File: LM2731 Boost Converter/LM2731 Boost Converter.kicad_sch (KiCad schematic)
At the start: 17 parts, among them J1 USB_C_Receptacle_PowerOnly_6P, SW1 SW_SPDT, U1 LM2731YMF

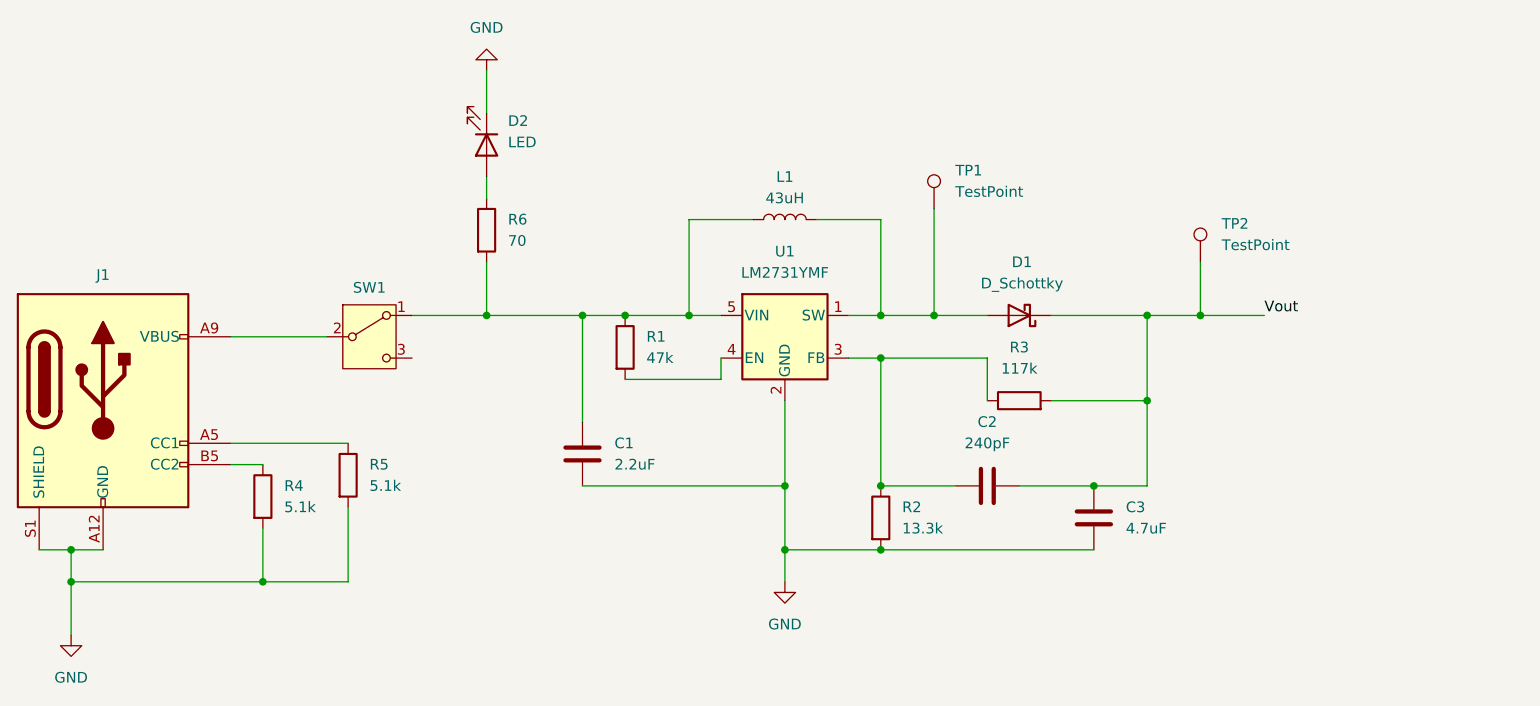
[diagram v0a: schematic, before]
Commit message: Finished sourcing parts and assigning footprints. Had to add the footprint for the inductor.
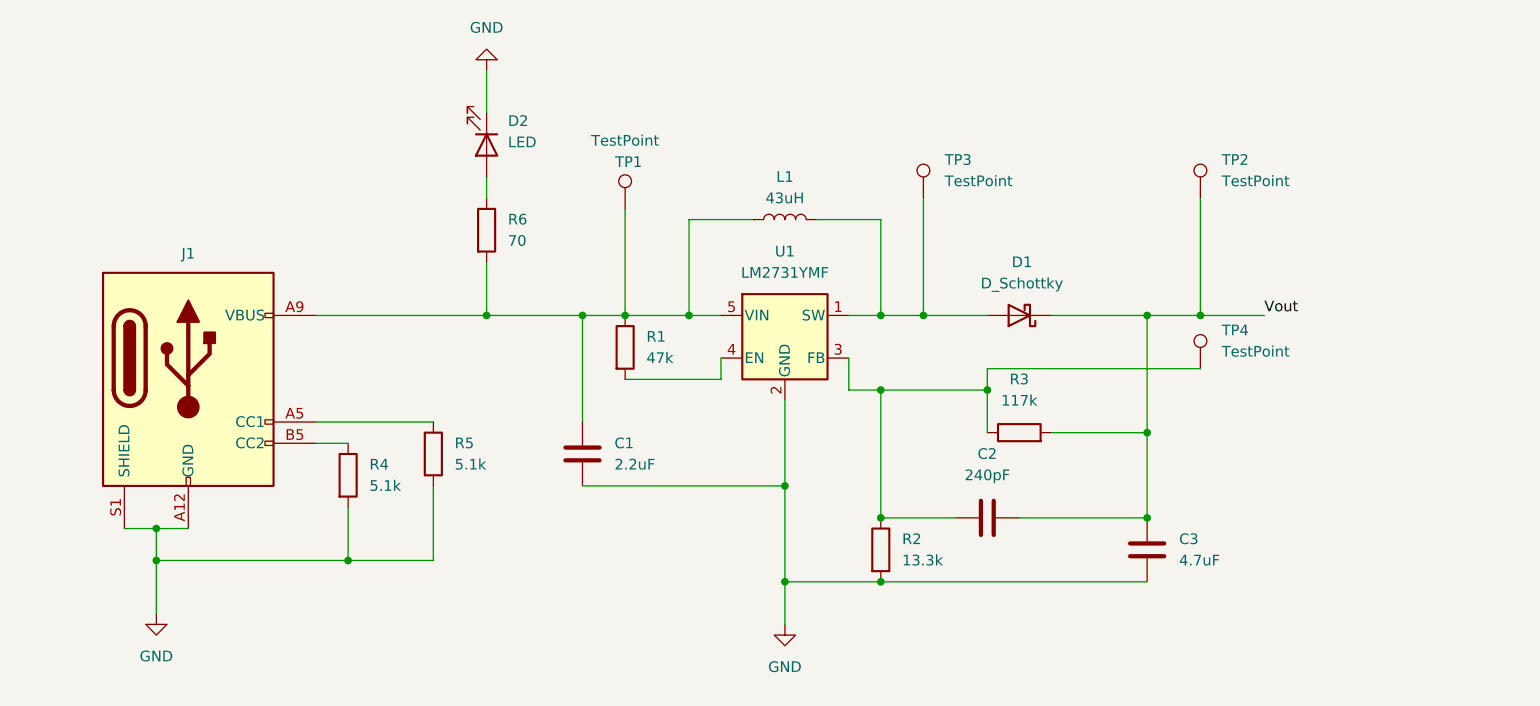
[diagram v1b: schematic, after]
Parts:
- removed SW1: SW_SPDT, symbol Switch:SW_SPDT
- added TP3, TP4: TestPoint, TestPoint:TestPoint_Keystone_5000-5004_Miniature, symbol Connector:TestPoint
- C1: Part Number  LMK316AB7226KL-TR -> LMF316B7225KLHT
- C2: footprint (none) -> Capacitor_SMD:C_0201_0603Metric_Pad0.64x0.40mm_HandSolder; Part Number  (none) -> KGM15AR71C221KT
- C3: footprint (none) -> Capacitor_SMD:C_1210_3225Metric_Pad1.33x2.70mm_HandSolder; Part Number  (none) -> LMK325BJ475KD-T
- L1: footprint (none) -> Inductor_SMD:IND_ASPI-8040S-430M-T; Part Number  (none) -> ASPI-8040S-430M-T
- R1: footprint (none) -> Resistor_SMD:R_0603_1608Metric_Pad0.98x0.95mm_HandSolder; Part Number  (none) -> RC0603FR-0747KL
- R2: footprint (none) -> Resistor_SMD:R_0603_1608Metric_Pad0.98x0.95mm_HandSolder; Part Number  (none) -> RC0603FR-0713K3L
- R3: footprint (none) -> Resistor_SMD:R_0603_1608Metric_Pad0.98x0.95mm_HandSolder; Part Number  (none) -> RT0603DRE07117KL
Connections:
- net at C1.1, L1.1, R1.1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: now also J1.A9 (VBUS), J1.B9 (VBUS), TP1.1
- net at D1.2 (A), L1.2, U1.1 (SW): now also TP3.1; no longer TP1.1
- net at C2.2, R2.1, R3.1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: now also TP4.1
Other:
- moved on the sheet: C2, C3, J1, R2, R3, R4, R5, TP1, TP2

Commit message: Started the PCB layout. Updated the Keystone 5000 test point to reflect the
correct part.
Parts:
- C2: footprint Capacitor_SMD:C_0201_0603Metric_Pad0.64x0.40mm_HandSolder -> Capacitor_SMD:C_0603_1608Metric_Pad1.08x0.95mm_HandSolder
- TP1, TP2, TP3, TP4: footprint TestPoint:TestPoint_Keystone_5000-5004_Miniature -> TestPoint:KEYSTONE_5000
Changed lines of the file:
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@@
 			)
 		)
-		(property "Footprint" "TestPoint:TestPoint_Keystone_5000-5004_Miniature"
+		(property "Footprint" "TestPoint:KEYSTONE_5000"
 			(at 180.34 71.12 0)
 			(effects
@@
 			)
 		)
-		(property "Footprint" "TestPoint:TestPoint_Keystone_5000-5004_Miniature"
+		(property "Footprint" "TestPoint:KEYSTONE_5000"
 			(at 213.36 91.44 0)
 			(effects
@@
 			)
 		)
-		(property "Footprint" "TestPoint:TestPoint_Keystone_5000-5004_Miniature"
+		(property "Footprint" "TestPoint:KEYSTONE_5000"
 			(at 144.78 72.39 0)
 			(effects
@@
 			)
 		)
-		(property "Footprint" "Capacitor_SMD:C_0201_0603Metric_Pad0.64x0.40mm_HandSolder"
+		(property "Footprint" "Capacitor_SMD:C_0603_1608Metric_Pad1.08x0.95mm_HandSolder"
 			(at 179.07 110.1852 0)
 			(effects
@@
 			)
 		)
-		(property "Footprint" "TestPoint:TestPoint_Keystone_5000-5004_Miniature"
+		(property "Footprint" "TestPoint:KEYSTONE_5000"
 			(at 213.36 71.12 0)
 			(effects

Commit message: Laid out parts and added a output screw terminal.
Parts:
- added J2: Screw_Terminal_01x02, TerminalBlock_Phoenix:PHOENIX_1725656, symbol Connector:Screw_Terminal_01x02
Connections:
- net GND: now also J2.2 (Pin_2)
- net Vout: now also J2.1 (Pin_1)
- net Vin: now reaches C1.1, J1.A9 (VBUS), J1.B9 (VBUS), L1.1, R1.1, R6.2, TP1.1, U1.5 (VIN)
- net SwitchNode: now reaches D1.2 (A), L1.2, TP3.1, U1.1 (SW)
- net Feedback: now reaches C2.2, R2.1, R3.1, TP4.1, U1.3 (FB)
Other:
- moved on the sheet: C2, C3, D1, R3, TP2, TP3, TP4

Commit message: Finished board layout.
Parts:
- U1: footprint Package_TO_SOT_SMD:SOT-23-5_HandSoldering -> Package_TO_SOT_SMD:SOT-23-5
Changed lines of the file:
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@@
 			)
 		)
-		(property "Footprint" "Package_TO_SOT_SMD:SOT-23-5_HandSoldering"
+		(property "Footprint" "Package_TO_SOT_SMD:SOT-23-5"
 			(at 160.02 93.98 0)
 			(effects
